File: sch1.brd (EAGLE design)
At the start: 108.9 x 88.9 mm, 44 parts, among them K1 351, K2 351, K3 351, K4 351, K5 351, K6 351

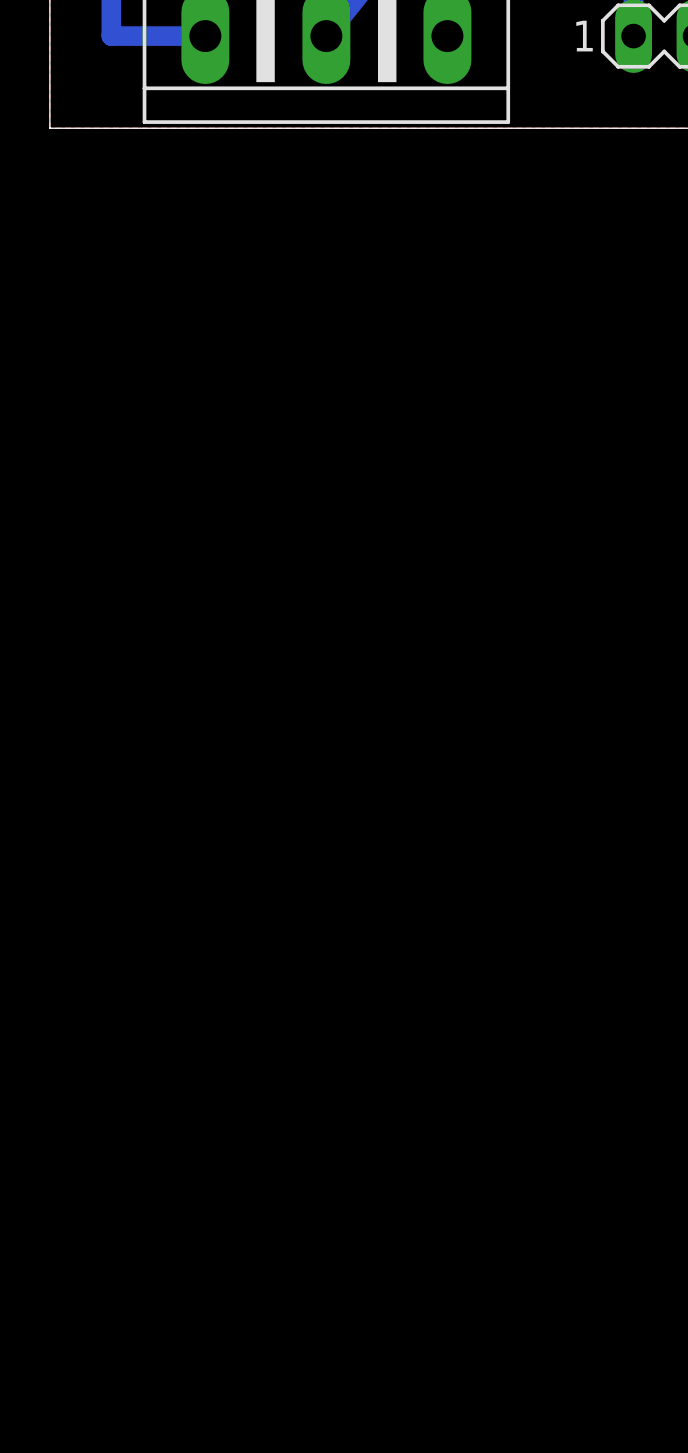
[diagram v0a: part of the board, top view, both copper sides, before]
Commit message: Added gainclone to scheme
Need to add control for mute relay
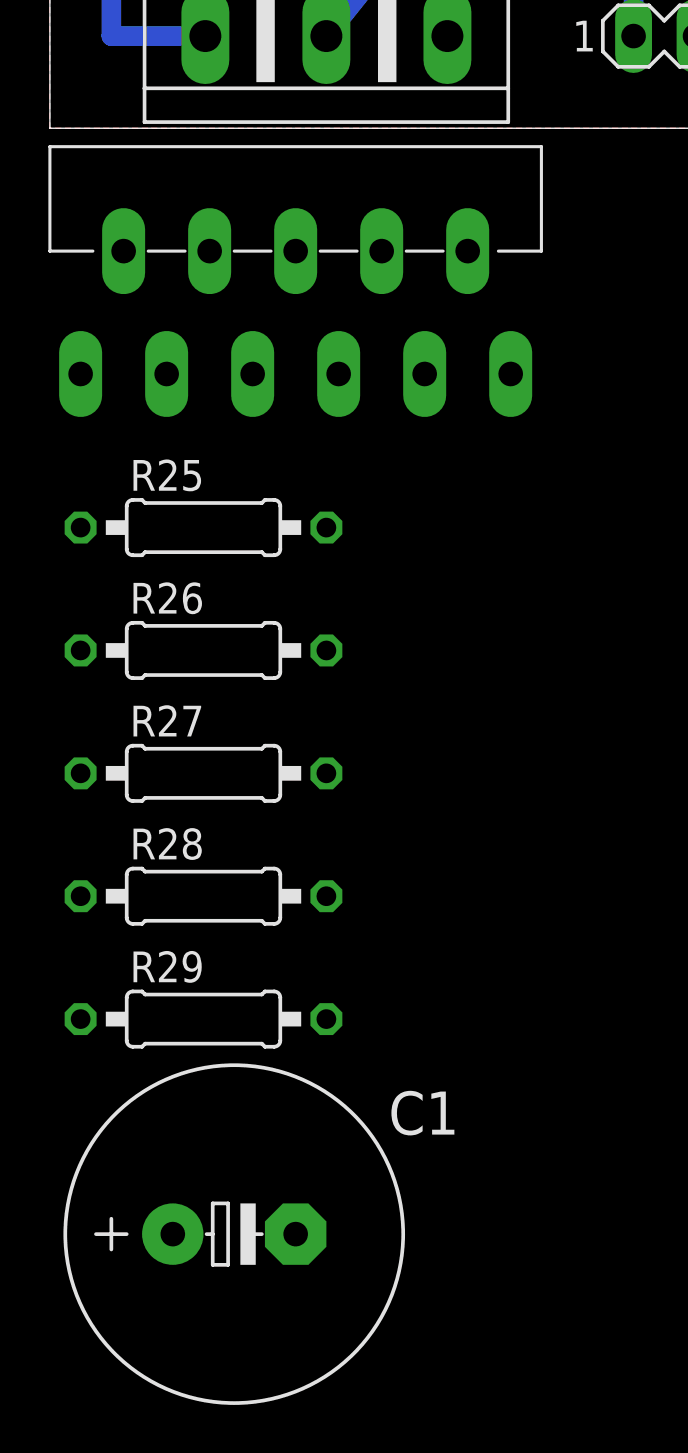
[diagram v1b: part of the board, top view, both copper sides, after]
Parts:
- added C1: (no value), rcl:E5-13
- added R25, R26, R27, R28, R29: (no value), rcl:0207/10
- added U$1: (no value), LM3886:TO220-11
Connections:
- new net 1: U$1.1
- new net 4: U$1.4
- new net 5: U$1.5
- new net 7: U$1.7
- new net N$47: R25.2, U$1.10
- new net N$48: R25.1
- new net N$51: U$1.9
- new net N$52: U$1.3
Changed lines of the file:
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@@
 <attribute name="OC_NEWARK" value="unknown" x="25.4" y="0" size="1.778" layer="27" display="off"/>
 </element>
+<element name="U$1" library="LM3886" package="TO220-11" value="" x="8.89" y="-11.43"/>
+<element name="R25" library="rcl" package="0207/10" value="" x="5.08" y="-20.32"/>
+<element name="R26" library="rcl" package="0207/10" value="" x="5.08" y="-25.4"/>
+<element name="R27" library="rcl" package="0207/10" value="" x="5.08" y="-30.48"/>
+<element name="R28" library="rcl" package="0207/10" value="" x="5.08" y="-35.56"/>
+<element name="R29" library="rcl" package="0207/10" value="" x="5.08" y="-40.64"/>
+<element name="C1" library="rcl" package="E5-13" value="" x="6.35" y="-49.53"/>
 </elements>
 <signals>
@@
 <contactref element="SV4" pad="3"/>
 </signal>
+<signal name="1">
+<contactref element="U$1" pad="1"/>
+</signal>
+<signal name="4">
+<contactref element="U$1" pad="4"/>
+</signal>
+<signal name="7">
+<contactref element="U$1" pad="7"/>
+</signal>
+<signal name="5">
+<contactref element="U$1" pad="5"/>
+</signal>
+<signal name="N$47">
+<contactref element="U$1" pad="10"/>
+<contactref element="R25" pad="2"/>
+<wire x1="16.002" y1="-8.89" x2="10.16" y2="-20.32" width="0" layer="19" extent="1-1"/>
+</signal>
+<signal name="N$48">
+<contactref element="R25" pad="1"/>
+</signal>
+<signal name="N$51">
+<contactref element="U$1" pad="9"/>
+</signal>
+<signal name="N$52">
+<contactref element="U$1" pad="3"/>
+</signal>
 </signals>
